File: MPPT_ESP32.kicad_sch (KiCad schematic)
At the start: 49 parts, among them J1 USB_C_Receptacle_USB2.0_16P, J2 Conn_01x05, SW1 SW_Push, SW2 SW_Push, SW3 SW_Push, SW4 SW_Push, SW5 SW_Push, SW6 SW_Push, U12 ADS1015IDGSR, U14 ESP32-S3(FN8), U19 W25Q128JVSIQTR, U20 ADS1015IDGSR, Y1 Crystal_GND24_Small

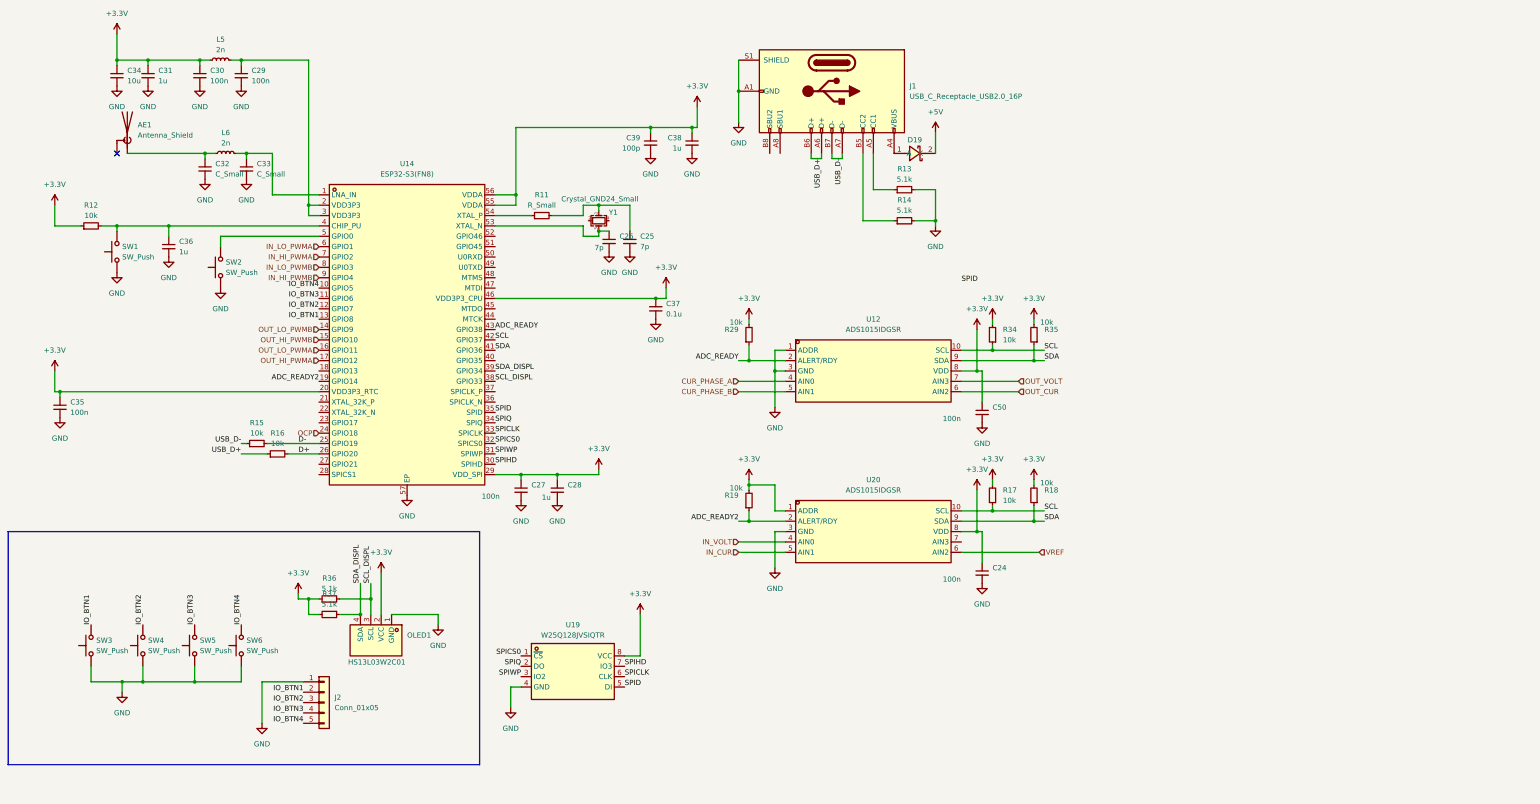
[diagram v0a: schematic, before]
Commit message: latest version with PWM fan and thermistors for each FET bank
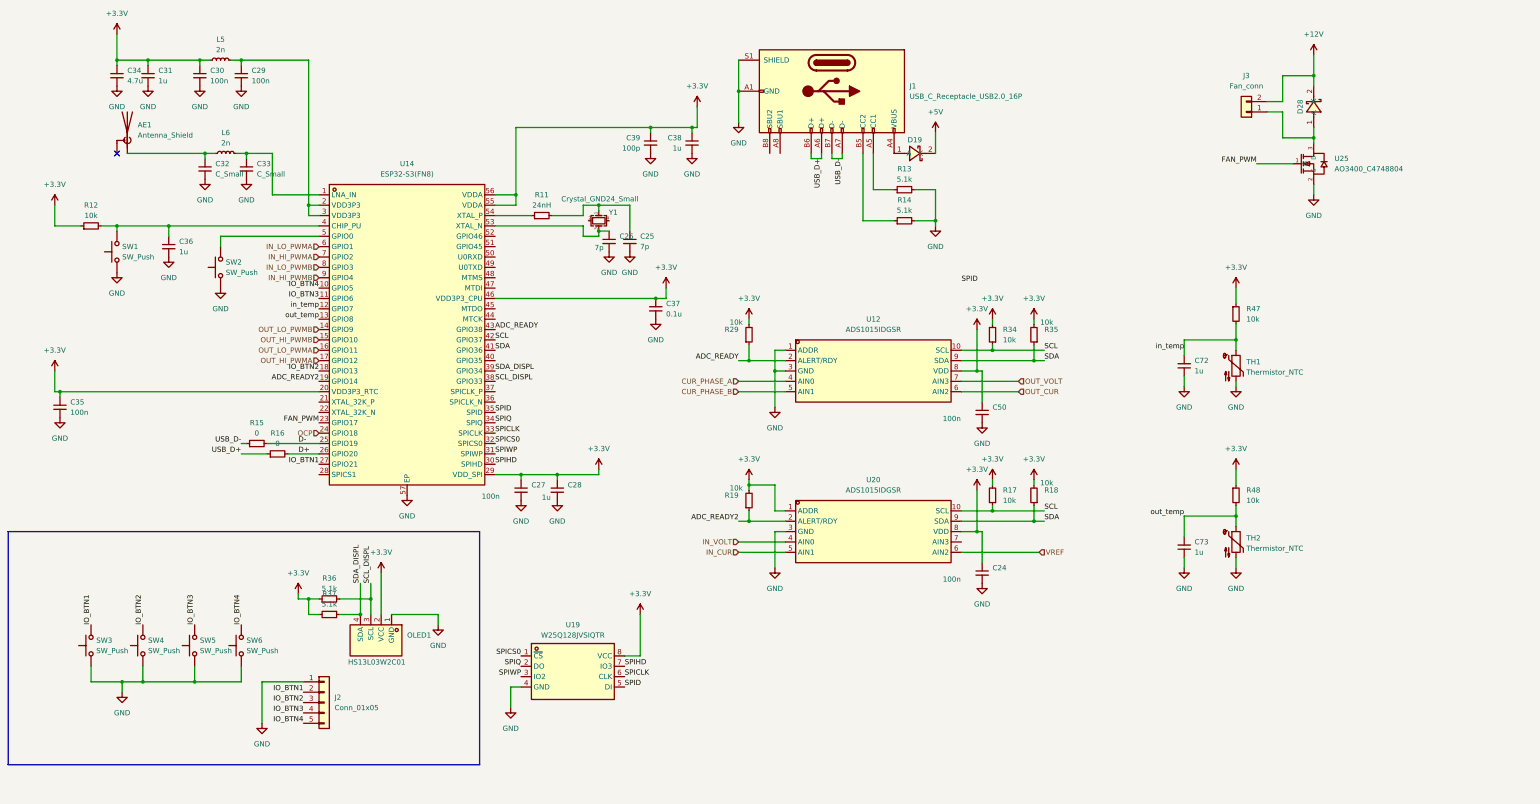
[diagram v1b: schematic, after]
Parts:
- added C72, C73: 1u, Capacitor_SMD:C_0402_1005Metric, symbol Device:C_Small
- added D28: B16WS_C7420327, easyeda2kicad:SOD-323_L1.7-W1.3-LS2.5-FD, symbol easyeda2kicad:B16WS_C7420327
- added J3: Fan_conn, symbol Connector_Generic:Conn_01x02
- added R47, R48: 10k, Resistor_SMD:R_0402_1005Metric, symbol Device:R_Small
- added TH1, TH2: Thermistor_NTC, Resistor_SMD:R_0402_1005Metric, symbol Device:Thermistor_NTC
- added U25: AO3400_C4748804, footprint:SOT-23_L2.9-W1.3-P1.90-LS2.4-BR, symbol easyeda2kicad2:AO3400_C4748804
- AE1: LCSC Part (none) -> C6807751
- C24, C50: footprint Resistor_SMD:R_0402_1005Metric -> Capacitor_SMD:C_0402_1005Metric; LCSC Part (none) -> C880603
- C25, C26: LCSC Part (none) -> C5448838
- C27, C29, C30, C35, C37: LCSC Part (none) -> C880603
- C28, C31, C38: LCSC Part (none) -> C466612
- C32, C33, J1, J2, OLED1, SW1, SW2, SW3, SW4, SW5, SW6: now left out of the parts list
- C34: value 10u -> 4.7u; LCSC Part (none) -> C20539423
- C36: footprint Resistor_SMD:R_0402_1005Metric -> Capacitor_SMD:C_0402_1005Metric; LCSC Part (none) -> C466612
- C39: LCSC Part (none) -> C541383
- L5, L6: LCSC Part (none) -> C18216
- R11: value R_Small -> 24nH; LCSC Part (none) -> C401493
- R12, R17, R18, R19, R29, R34, R35: LCSC Part (none) -> C60490
- R13, R14, R36, R37: LCSC Part (none) -> C25905
- R15, R16: value 10k -> 0; LCSC Part (none) -> C3017451
- Y1: LCSC Part (none) -> C700790
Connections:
- net +3.3V: now also R47.1, R48.1
- net GND: now also C72.1, C73.1, TH1.2, TH2.2, U25.2 (S)
- net IO_BTN1: now also U14.27 (GPIO21); no longer U14.13 (GPIO8)
- net IO_BTN2: now also U14.18 (GPIO13); no longer U14.12 (GPIO7)
- net FAN_PWM: now reaches U14.23 (GPIO17)
- net FAN_PWM: now also U25.1 (G)
- new net: D28.1 (A), J3.1 (Pin_1), U25.3 (D)
- new net +12V: D28.2 (K), J3.2 (Pin_2)
- new net in_temp: C72.2, R47.2, TH1.1, U14.12 (GPIO7)
- new net out_temp: C73.2, R48.2, TH2.1, U14.13 (GPIO8)

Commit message: production version v3
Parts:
- added J5: Fan_conn, Connector_PinHeader_2.54mm:PinHeader_1x02_P2.54mm_Vertical, symbol Connector_Generic:Conn_01x02
- added R50, R51: 0, Resistor_SMD:R_0402_1005Metric, symbol Device:R_Small
- added U27: SN65HVD234DR, footprint:SOIC-8_L4.9-W3.9-P1.27-LS6.0-BL, symbol easyeda2kicad2:SN65HVD234DR
- J3: footprint (none) -> Connector_PinHeader_2.54mm:PinHeader_1x02_P2.54mm_Vertical
- Y1: footprint Crystal:Crystal_SMD_SeikoEpson_FA238V-4Pin_3.2x2.5mm -> Crystal:Crystal_SMD_SeikoEpson_FA238-4Pin_3.2x2.5mm
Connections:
- net +3.3V: now also R51.2, U27.3 (VCC)
- net FAN_PWM: now also U14.40 (GPIO35); no longer U14.23 (GPIO17)
- net GND: now also R50.1, U27.2 (GND)
- net CAN_TX: now reaches U14.49 (U0TXD)
- net CAN_TX: now also U27.1 (D)
- net CAN_RX: now reaches U14.50 (U0RXD)
- net CAN_RX: now also U27.4 (R)
- new net: R51.1, U27.5 (EN)
- new net: J5.1 (Pin_1), U27.7 (CANH)
- new net: J5.2 (Pin_2), U27.6 (CANL)
- new net: R50.2, U27.8 (RS)
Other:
- moved on the sheet: C24, C50, C72, C73, R17, R18, R19, R29, R34, R35, R47, R48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
